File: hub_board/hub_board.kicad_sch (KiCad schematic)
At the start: 15 parts, among them J1 Fingers, J2 Fingers, J3 Fingers, J4 Fingers, J5 1473149-4, J6 Test Points, J7 54-00166, U1 AP2112K-3.3TRG1

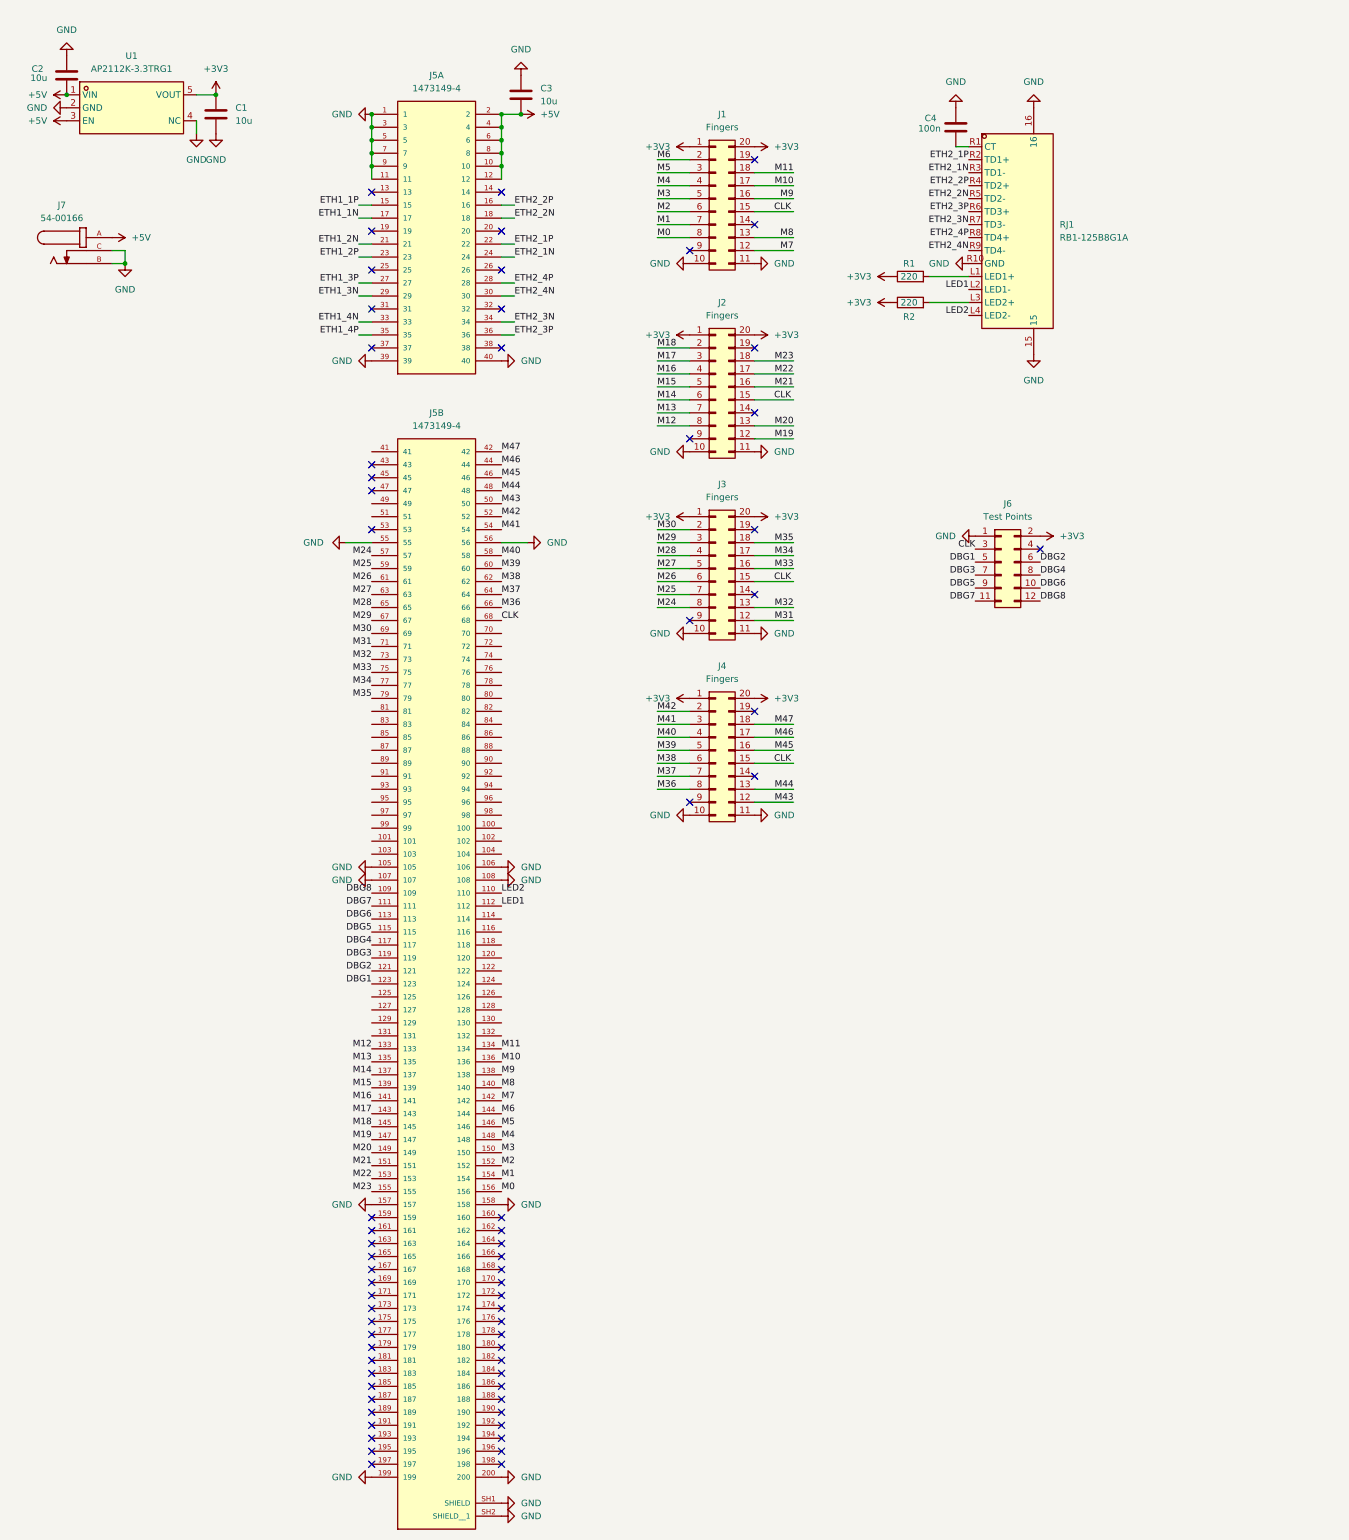
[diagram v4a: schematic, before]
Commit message: Finish routing hub board
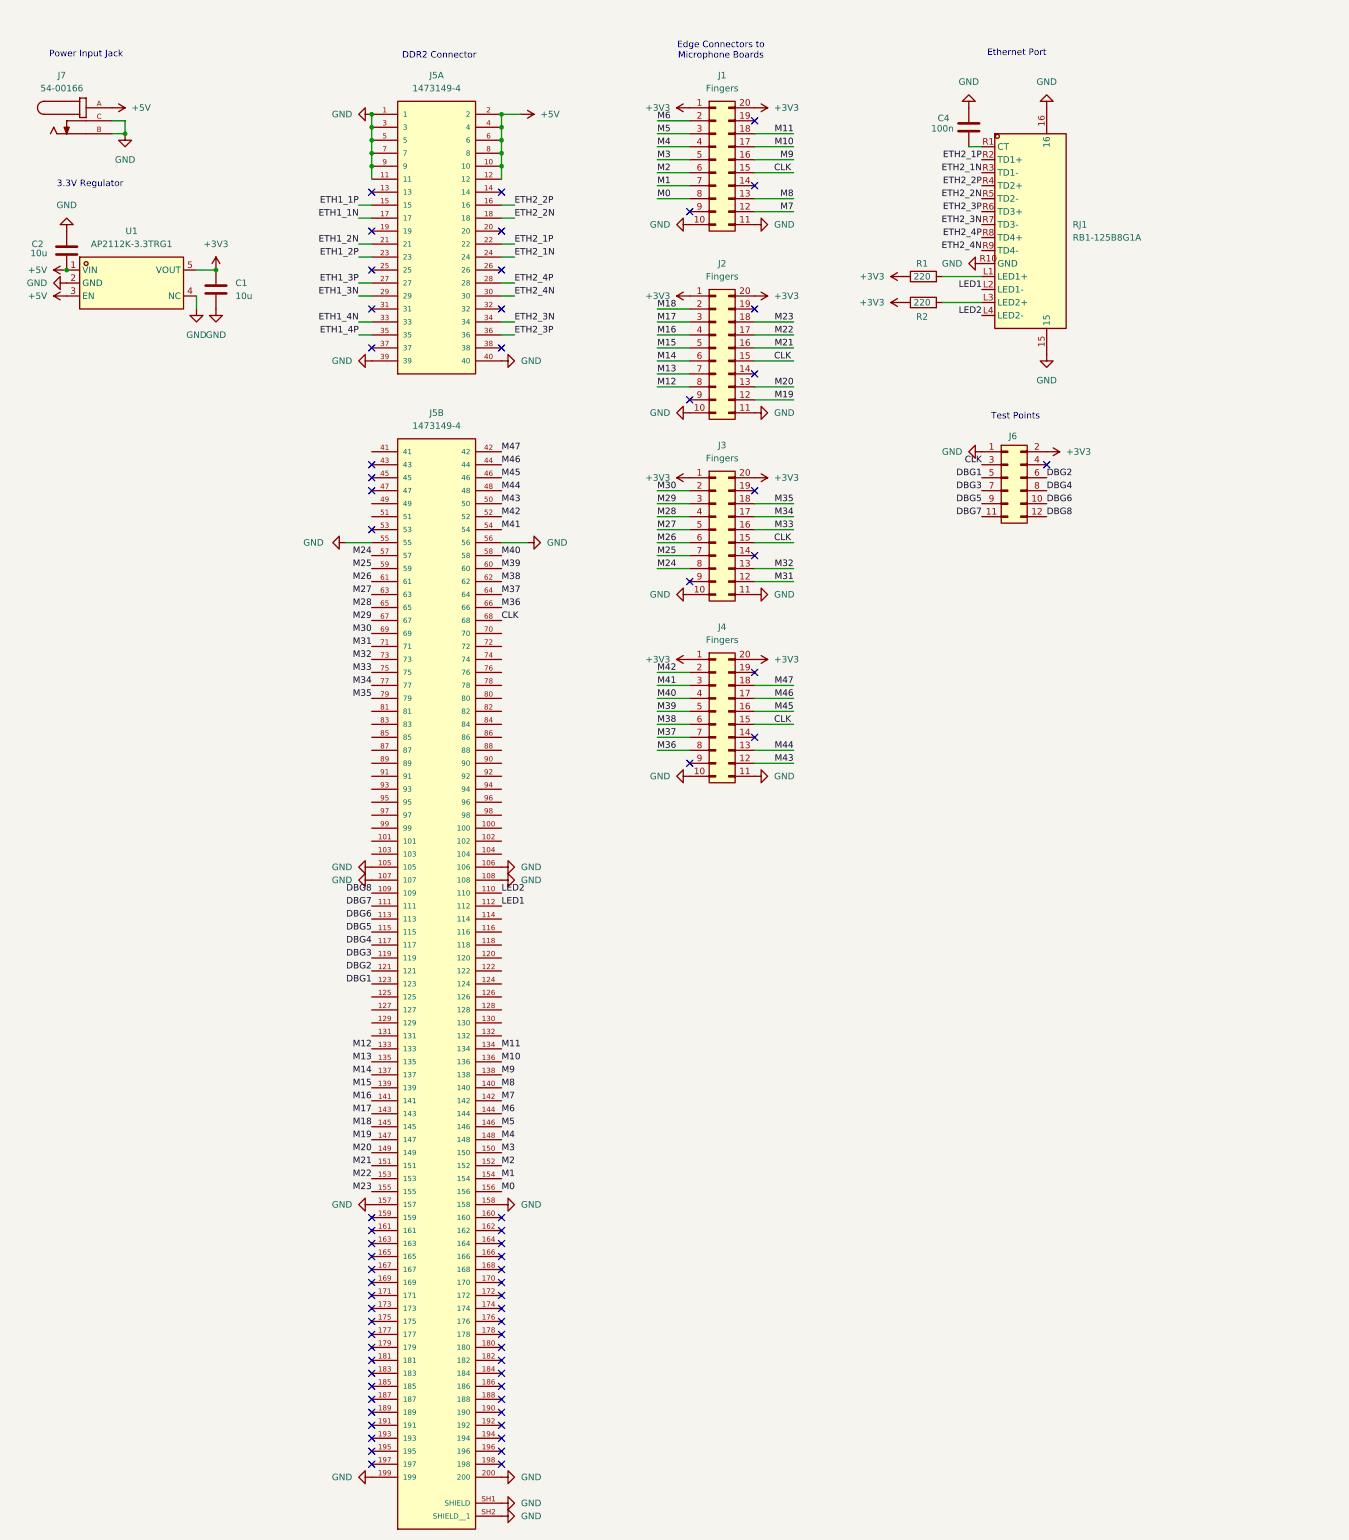
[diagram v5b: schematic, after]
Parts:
- removed C3: 10u, symbol Device:C
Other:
- note added: "3.3V Regulator"
- note added: "DDR2 Connector"
- note added: "Edge Connectors to Microphone Boards"
- note added: "Ethernet Port"
- note added: "Power Input Jack"
- note added: "Test Points"
- moved on the sheet: C1, C2, C4, J1, J2, J3, J4, J6, J7, R1, R2, RJ1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
